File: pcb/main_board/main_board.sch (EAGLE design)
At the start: 30 parts, among them J1 5025700893, P1 53398-0510, P2 53398-0810, P3 53398-0410, U1 ATSAMD51J19A-AUT, U13 SPX3819-3.3, X2 32.768, X3 microUSB

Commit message: moved to feather wing design
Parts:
- removed C10: 1uF, rcl:C-EUC0603
- removed C6, C7, C8: 0.1uF, rcl:C-EUC0603
- removed C9: 0.01uF, rcl:C-EUC0603
- removed D1: MBR120, microbuilder:DIODE-SCHOTTKYSOD-123
- removed H1, H2, H3, H4: MOUNT-PAD-ROUND3.0, holes:MOUNT-PAD-ROUND3.0
- removed J1: 5025700893, 5025700893:5025700893
- removed L2: 10uH, microbuilder:INDUCTOR
- removed P2: 53398-0810, con-molex-picoblade:53398-0810
- removed P3: 53398-0410, con-molex-picoblade:53398-0410
- removed U$34: MAX3232E, TI_radio:MAX3232E
- removed X2: 32.768, adafruit2:XTAL-3.2X1.5
- removed X3: microUSB, microbuilder:USB_MICRO_20329_V2
- added C02_SERVO, IMU: 53398-0310, con-molex-picoblade:53398-0310
- added C14: 0.1uF, adafruit:C-USC0603
- added GPS, I2C, IRIDIUM: 53398-0410, con-molex-picoblade:53398-0410
- added JP1: (no value), microbuilder:HEADER-1X16ROUND
- added JP3: (no value), microbuilder:HEADER-1X12
- added PYRO, PYRO_BAT: 53398-0210, con-molex-picoblade:53398-0210
- added R3: 288, adafruit:R-US_R0603
- added SD_CARD: DM3CS-SF, DM3CS-SF:DM3CS-SF
- added TPMS: 53398-0610, con-molex-picoblade:53398-0610
- added U$1, U$7: AQV252GA, TI_radio:AQV252GA
- C1: value 1uF -> 0.1uF
- C2: value 10uF -> 0.1uF; device rcl:C-EUC0805 -> rcl:C-EUC0603
- C3, C4: value 22pF -> 0.1uF; device microbuilder:CAP_CERAMIC0603_NO -> rcl:C-EUC0603
- C5: device rcl:C-EUC0603 -> adafruit:C-USC0603
- R1: value 10k -> 288; device rcl:R-EU_R0603 -> adafruit:R-US_R0603
- U1: value ATSAMD51J19A-AUT -> ADM3101EARQZ-REELRQ_16_ADI-L; device ATSAMD51J19A-AUT:ATSAMD51J19A-AUT -> ADM310:ADM3101EARQZ-REELRQ_16_ADI-L
- renumbered P1 to TELEM
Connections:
- removed net 3.3V: C7.1, U$34.VCC
- removed net D+: U1.PA25/EIC/EXTINT[9], X3.D+
- removed net D-: U1.PA24/EIC/EXTINT[8], X3.D-
- removed net N$11: J1.DAT3/CD
- removed net N$12: J1.DAT2
- removed net N$13: J1.DAT1
- removed net N$14: J1.DAT0
- removed net N$15: TELEM.2
- removed net N$16: TELEM.3
- removed net N$17: TELEM.4
- removed net N$18: TELEM.5
- removed net N$19: H2.MOUNT
- removed net N$2: TELEM.1
- removed net N$20: H1.MOUNT
- removed net N$21: H4.MOUNT
- removed net N$22: H3.MOUNT
- removed net N$23: P2.1
- removed net N$24: P2.2
- removed net N$25: P2.3
- removed net N$26: P2.4
- removed net N$27: P2.5
- removed net N$28: P2.6
- removed net N$29: P2.7
- removed net N$30: P2.8
- removed net N$31: P3.1
- removed net N$32: P3.2
- removed net N$33: P3.3
- removed net N$34: P3.4
- removed net N$35: C5.1, U$34.C1+
- removed net N$36: C5.2, U$34.C1-
- removed net N$37: C8.1, U$34.C2+
- removed net N$38: C8.2, U$34.C2-
- removed net N$39: C9.1, U$34.V-
- removed net N$40: C6.1, U$34.V+
- removed net N$41: C10.2, U1.PA03/EIC/EXTINT[3]/ANAREF/VREFA/ADC0/ADIN[1]
- removed net N$5: C3.1, U1.PA00/EIC/EXTINT[0], X2.P$1
- removed net QSPI_CS: U1.PB11//EIC/EXTINT[11]
- removed net QSPI_DATA[0]: U1.PA08/EIC/NMI/ADC0/AIN[8]/ADC1/AIN[2]
- removed net QSPI_DATA[1]: U1.PA09/EIC/EXTINT[9]/ADC0/AIN[9]/ADC1/AIN[3]
- removed net QSPI_DATA[2]: U1.PA10//EIC/EXTINT[10]/ADC0/AIN[10]
- removed net QSPI_DATA[3]: U1.PA11/EIC/EXTINT[11]/ADC0/AIN[11]
- removed net QSPI_SCK: U1.PB10/EIC/EXTINT[10]
- removed net RX0: U1.PB17/EIC/EXTINT[1]
- removed net SD_DET: J1.DET_SW
- removed net SWCLK: U1.PA30//EIC/EXTINT[14]/X19/Y19
- removed net SWDIO: U1.PA31//EIC/EXTINT[15]
- removed net TX0: U1.PB16/EIC/EXTINT[0]
- new net !RESET: JP1.16
- new net 3V32: C29.1, C30.1, TELEM.4, U13.OUT
- new net 9V: PYRO_BAT.1, U$1.P$6
- new net AREF: JP1.14
- new net CO2_SERVO: C02_SERVO.1, JP3.6
- new net D5: JP3.10
- new net D6: JP3.9
- new net IR_ACT: JP3.7, R3.2
- new net LORA_RST: JP1.12, TELEM.1
- new net MISO: JP1.4, SD_CARD.DAT0
- new net MOSI: JP1.5, SD_CARD.CMD
- new net N$1: C5.1, R1.1, U$1.P$1
- new net N$6: C14.1, R3.1, U$7.P$1
- new net PYRO_ACT: JP3.8, R1.2
- new net RX4: JP1.11, TELEM.3
- new net SCHED: JP1.1, TPMS.2
- new net SCK: JP1.6, SD_CARD.CLK
- new net SCL: I2C.1, JP3.11
- new net SDA: I2C.2, JP3.12
- new net SD_CS: JP1.7, SD_CARD.CD/DAT3
- new net TX4: JP1.8, TELEM.2
- new net V+_IRIDIUM: IRIDIUM.3, U$7.P$4
- new net V+_PYRO: PYRO.1, U$1.P$4
- net 3V3: now also C4.2, GPS.3, I2C.3, JP1.15, SD_CARD.VDD, U1.VCC; no longer C29.1, C30.1, R1.2, U1.VDDANA, U1.VDDIO, U13.OUT
- net EN: now also IMU.1, JP3.2, TPMS.1
- net GND: now also C02_SERVO.3, C14.2, C5.2, GPS.4, I2C.4, IMU.3, IRIDIUM.4, JP1.13, PYRO.2, PYRO_BAT.2, SD_CARD.GND, SD_CARD.VSS, TELEM.5, TPMS.6, U$1.P$2, U$7.P$2; no longer C1.2, C10.1, C2.2, C4.2, C6.2, C7.2, C9.2, J1.DET_LEVER, J1.VSS, R1.1, U$34.GND, U1.RESETN, X3.GND
- net N$10: now also C2.2, U1.C2-; no longer J1.CMD
- net N$3: now also C4.1, U1.V+; no longer L2.1, U1.VSW
- net N$4: now also C3.1, U1.V-; no longer C1.1, C2.1, L2.2, U1.VDDCORE
- net N$7: now also C2.1, U1.C2+; no longer C4.1, U1.PA01/EIC/EXTINT[1], X2.P$2
- net N$8: now also C1.1, U1.C1+; no longer J1.VDD
- net N$9: now also C1.2, U1.C1-; no longer J1.CLK
- net R232: now also IRIDIUM.2, U1.RIN; no longer U$34.RI2
- net RIRI: now also JP3.4, U1.ROUT; no longer U$34.RO2
- net RX1: now also JP1.3, TPMS.4; no longer U1.PB09/EIC/EXTINT[9]/ADC0/AIN[3]/ADC1/AIN[1]
- net RX2: now also GPS.1, JP1.9; no longer U1.PA05//EIC/EXTINT[5]/ADC0/AIN[5]
- net T232: now also IRIDIUM.1, U1.TOUT; no longer U$34.DO2
- net TIRI: now also JP3.5, U1.TIN; no longer U$34.DI2
- net TX1: now also JP1.2, TPMS.3; no longer U1.PB08/EIC/EXTINT[8]/ADC0/AIN[2]/ADC1/AIN[0]
- net TX2: now also GPS.2, JP1.10; no longer U1.PA04/EIC/EXTINT[4]/ANAREF/VREFB/ADOC0/AIN[4]
- net VBAT: now also C02_SERVO.2, C22.1, IMU.2, JP3.1, R45.1, TPMS.5, U$7.P$6, U13.IN; no longer D1.A
- net VBUS: now also JP3.3; no longer C22.1, D1.C, R45.1, U13.IN, X3.VBUS
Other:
- note added: "BREAKOUTS"
- note added: "Solid State Relay"
- note removed: "3v3 ttl cons"
- note removed: "Iridium"
- note removed: "RS232 Connections"

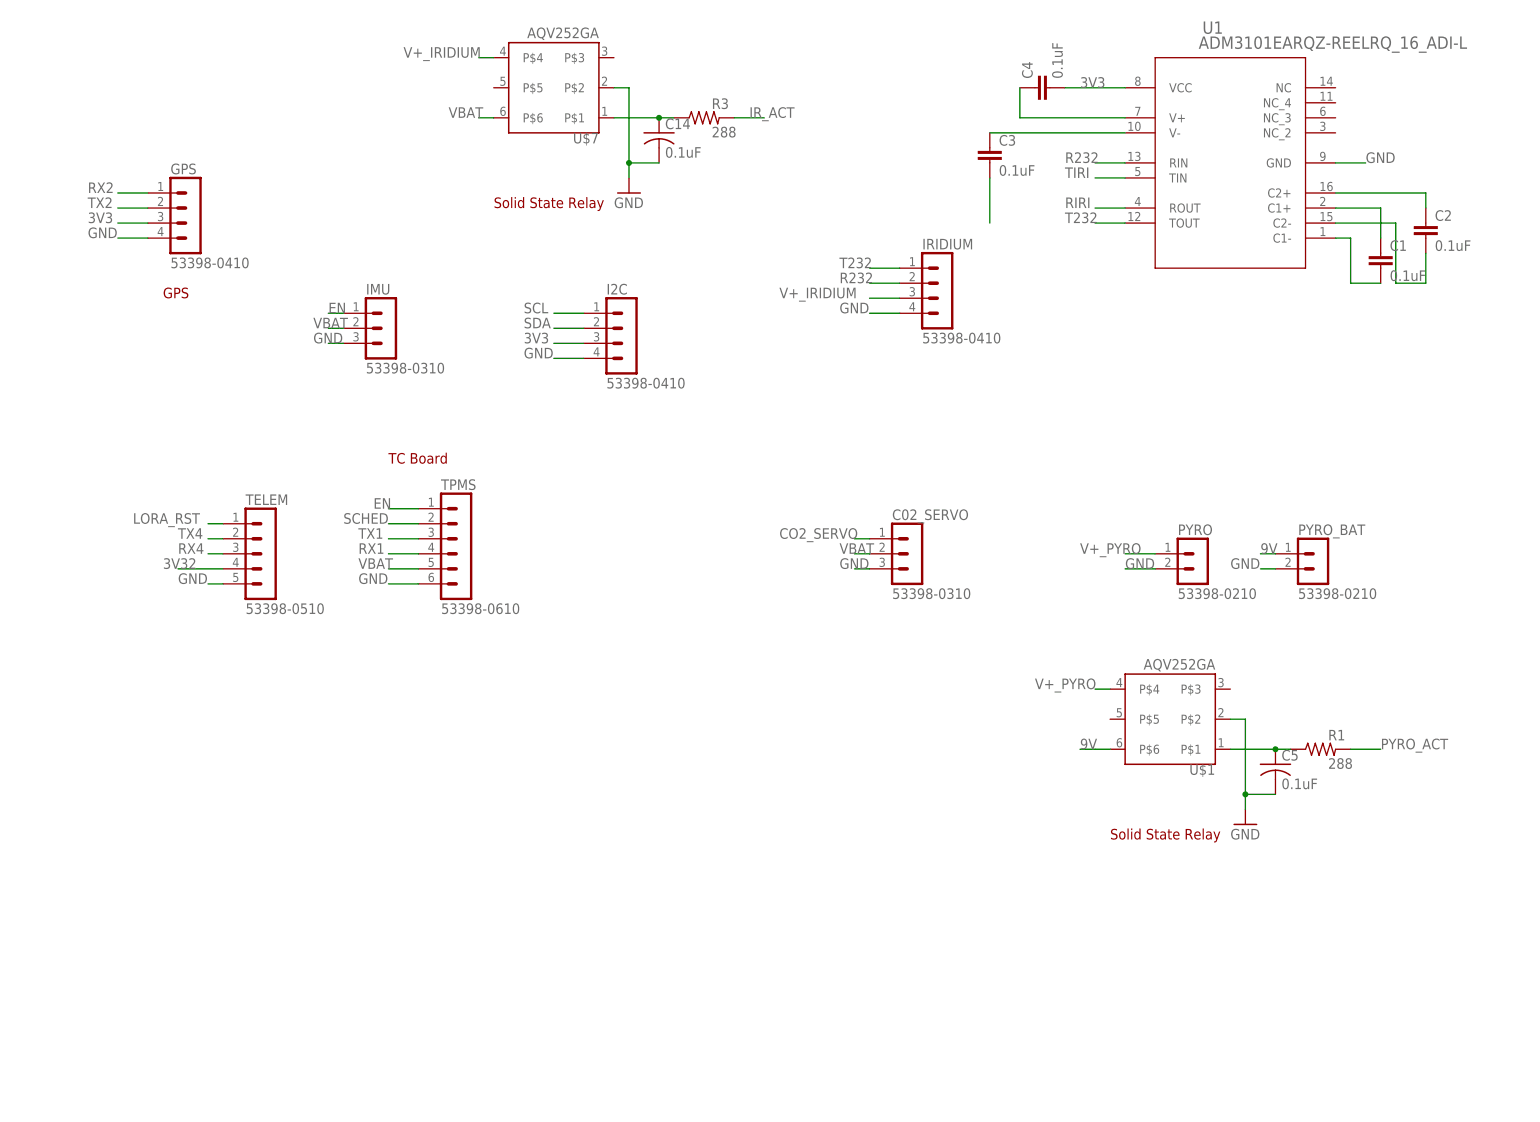
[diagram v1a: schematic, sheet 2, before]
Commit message: initial versions of imu logger, cdh, and tpms pcb
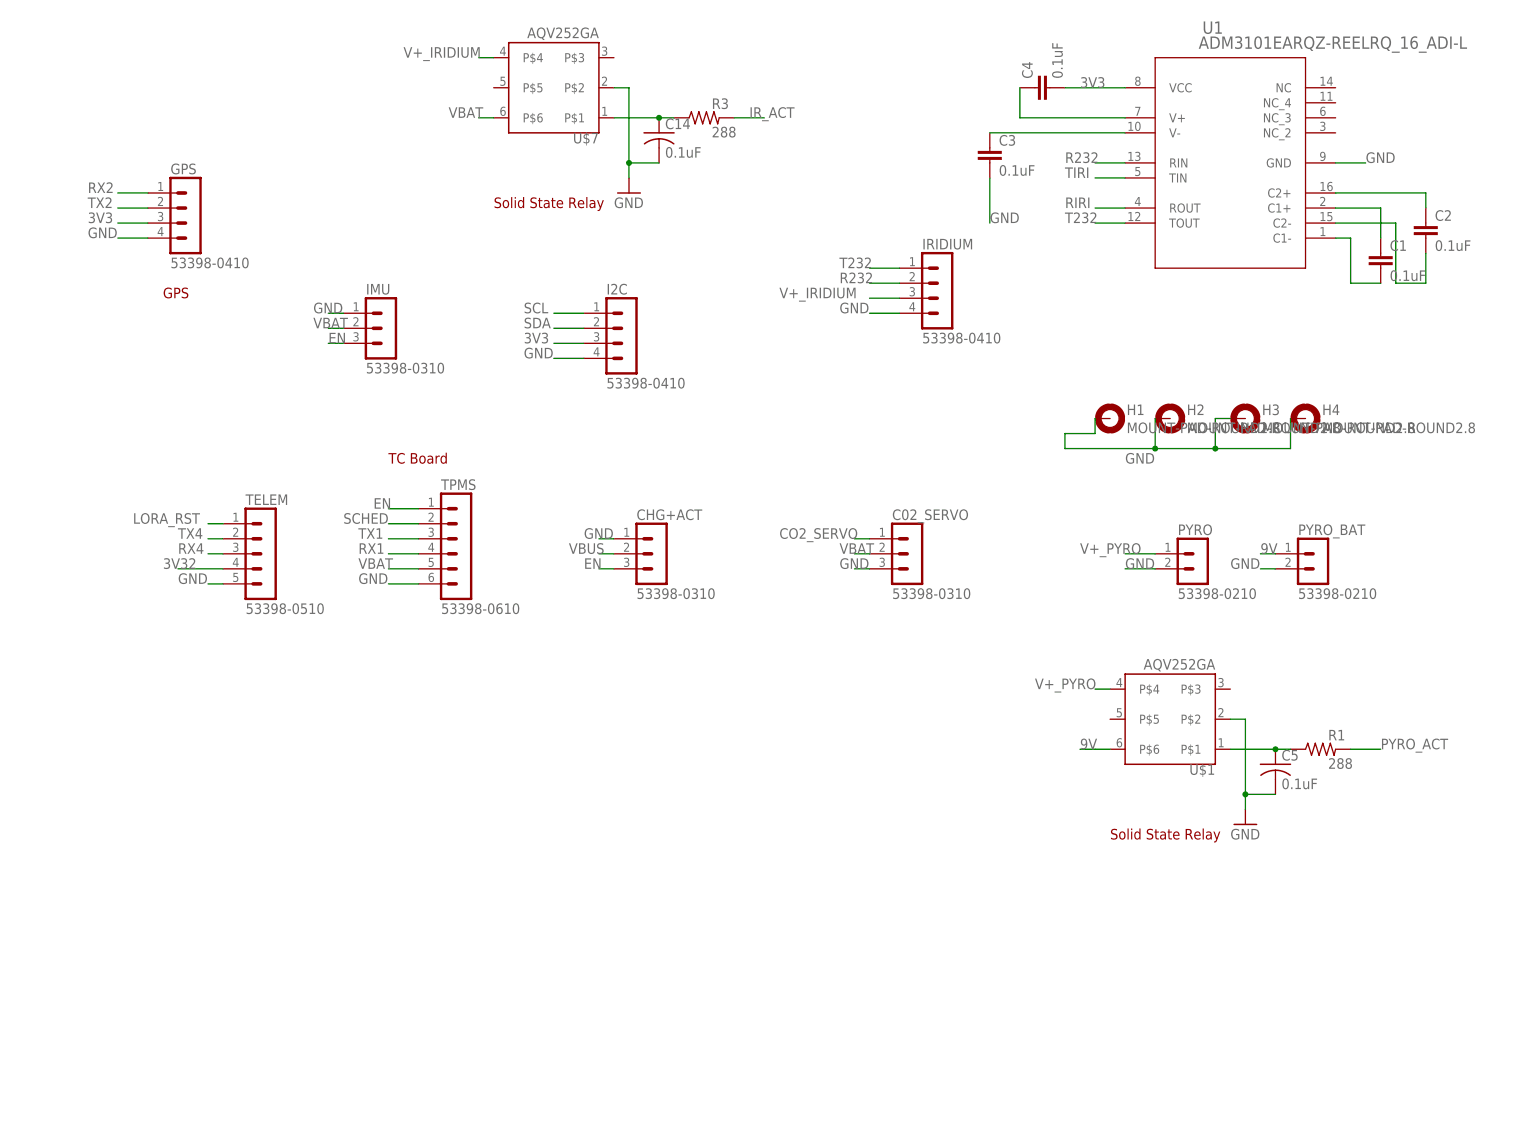
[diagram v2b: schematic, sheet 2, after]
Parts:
- added CHG+ACT: 53398-0310, con-molex-picoblade:53398-0310
- added H1, H2, H3, H4: MOUNT-PAD-ROUND2.8, holes:MOUNT-PAD-ROUND2.8
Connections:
- net EN: now also CHG+ACT.3, IMU.3; no longer IMU.1
- net GND: now also CHG+ACT.1, H1.MOUNT, H2.MOUNT, H3.MOUNT, H4.MOUNT, IMU.1; no longer IMU.3
- net VBUS: now also CHG+ACT.2
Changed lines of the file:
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@@
 <part name="U13" library="microbuilder" deviceset="VREG_SOT23-5" device="" value="SPX3819-3.3"/>
 <part name="R45" library="microbuilder" deviceset="RESISTOR" device="_0603_NOOUT" value="100k"/>
+<part name="H1" library="holes" library_urn="urn:adsk.eagle:library:237" deviceset="MOUNT-PAD-ROUND" device="2.8" package3d_urn="urn:adsk.eagle:package:14281/1"/>
+<part name="H2" library="holes" library_urn="urn:adsk.eagle:library:237" deviceset="MOUNT-PAD-ROUND" device="2.8" package3d_urn="urn:adsk.eagle:package:14281/1"/>
+<part name="H3" library="holes" library_urn="urn:adsk.eagle:library:237" deviceset="MOUNT-PAD-ROUND" device="2.8" package3d_urn="urn:adsk.eagle:package:14281/1"/>
+<part name="H4" library="holes" library_urn="urn:adsk.eagle:library:237" deviceset="MOUNT-PAD-ROUND" device="2.8" package3d_urn="urn:adsk.eagle:package:14281/1"/>
+<part name="CHG+ACT" library="con-molex-picoblade" library_urn="urn:adsk.eagle:library:28185481" deviceset="53398-0310" device="" package3d_urn="urn:adsk.eagle:package:28185543/1"/>
 </parts>
 <sheets>
@@
 <attribute name="VALUE" x="217.17" y="86.36" size="1.778" layer="95"/>
 </instance>
+<instance part="H1" gate="G$1" x="185.42" y="116.84" smashed="yes">
+<attribute name="NAME" x="188.214" y="117.4242" size="1.778" layer="95"/>
+<attribute name="VALUE" x="188.214" y="114.3762" size="1.778" layer="96"/>
+</instance>
+<instance part="H2" gate="G$1" x="195.58" y="116.84" smashed="yes">
+<attribute name="NAME" x="198.374" y="117.4242" size="1.778" layer="95"/>
+<attribute name="VALUE" x="198.374" y="114.3762" size="1.778" layer="96"/>
+</instance>
+<instance part="H3" gate="G$1" x="208.28" y="116.84" smashed="yes">
+<attribute name="NAME" x="211.074" y="117.4242" size="1.778" layer="95"/>
+<attribute name="VALUE" x="211.074" y="114.3762" size="1.778" layer="96"/>
+</instance>
+<instance part="H4" gate="G$1" x="218.44" y="116.84" smashed="yes">
+<attribute name="NAME" x="221.234" y="117.4242" size="1.778" layer="95"/>
+<attribute name="VALUE" x="221.234" y="114.3762" size="1.778" layer="96"/>
+</instance>
+<instance part="CHG+ACT" gate="G$1" x="106.68" y="93.98" smashed="yes">
+<attribute name="NAME" x="105.41" y="99.695" size="1.778" layer="95"/>
+<attribute name="VALUE" x="105.41" y="86.36" size="1.778" layer="95"/>
+</instance>
 </instances>
 <busses>
@@
 <pinref part="C3" gate="G$1" pin="2"/>
 <wire x1="165.1" y1="157.48" x2="165.1" y2="149.86" width="0.1524" layer="91"/>
+<label x="165.1" y="149.86" size="1.778" layer="95"/>
 </segment>
 <segment>
@@
 <wire x1="35.56" y1="88.9" x2="33.02" y2="88.9" width="0.1524" layer="91"/>
 <label x="27.94" y="88.9" size="1.778" layer="95"/>
-</segment>
-<segment>
-<pinref part="IMU" gate="G$1" pin="3"/>
-<wire x1="55.88" y1="129.54" x2="53.34" y2="129.54" width="0.1524" layer="91"/>
-<label x="50.8" y="129.54" size="1.778" layer="95"/>
 </segment>
 <segment>
@@
 <label x="205.74" y="91.44" size="1.778" layer="95"/>
 </segment>
+<segment>
+<pinref part="H1" gate="G$1" pin="MOUNT"/>
+<wire x1="182.88" y1="116.84" x2="182.88" y2="114.3" width="0.1524" layer="91"/>
+<wire x1="182.88" y1="114.3" x2="177.8" y2="114.3" width="0.1524" layer="91"/>
+<wire x1="177.8" y1="114.3" x2="177.8" y2="111.76" width="0.1524" layer="91"/>
+<wire x1="177.8" y1="111.76" x2="193.04" y2="111.76" width="0.1524" layer="91"/>
+<pinref part="H2" gate="G$1" pin="MOUNT"/>
+<wire x1="193.04" y1="111.76" x2="193.04" y2="116.84" width="0.1524" layer="91"/>
+<wire x1="193.04" y1="111.76" x2="203.2" y2="111.76" width="0.1524" layer="91"/>
+<junction x="193.04" y="111.76"/>
+<pinref part="H3" gate="G$1" pin="MOUNT"/>
+<wire x1="203.2" y1="111.76" x2="203.2" y2="116.84" width="0.1524" layer="91"/>
+<wire x1="203.2" y1="116.84" x2="205.74" y2="116.84" width="0.1524" layer="91"/>
+<wire x1="203.2" y1="111.76" x2="215.9" y2="111.76" width="0.1524" layer="91"/>
+<junction x="203.2" y="111.76"/>
+<pinref part="H4" gate="G$1" pin="MOUNT"/>
+<wire x1="215.9" y1="111.76" x2="215.9" y2="116.84" width="0.1524" layer="91"/>
+<label x="187.96" y="109.22" size="1.778" layer="95"/>
+</segment>
+<segment>
+<pinref part="IMU" gate="G$1" pin="1"/>
+<wire x1="55.88" y1="134.62" x2="53.34" y2="134.62" width="0.1524" layer="91"/>
+<label x="50.8" y="134.62" size="1.778" layer="95"/>
+</segment>
+<segment>
+<pinref part="CHG+ACT" gate="G$1" pin="1"/>
+<wire x1="101.6" y1="96.52" x2="99.06" y2="96.52" width="0.1524" layer="91"/>
+<label x="96.52" y="96.52" size="1.778" layer="95"/>
+</segment>
 </net>
 <net name="RIRI" class="0">
@@
 </segment>
 <segment>
-<pinref part="IMU" gate="G$1" pin="1"/>
-<wire x1="55.88" y1="134.62" x2="53.34" y2="134.62" width="0.1524" layer="91"/>
-<label x="53.34" y="134.62" size="1.778" layer="95"/>
+<pinref part="IMU" gate="G$1" pin="3"/>
+<wire x1="55.88" y1="129.54" x2="53.34" y2="129.54" width="0.1524" layer="91"/>
+<label x="53.34" y="129.54" size="1.778" layer="95"/>
+</segment>
+<segment>
+<pinref part="CHG+ACT" gate="G$1" pin="3"/>
+<wire x1="101.6" y1="91.44" x2="99.06" y2="91.44" width="0.1524" layer="91"/>
+<label x="96.52" y="91.44" size="1.778" layer="95"/>
 </segment>
 </net>
@@
 </segment>
 </net>
+<net name="VBUS" class="0">
+<segment>
+<pinref part="CHG+ACT" gate="G$1" pin="2"/>
+<wire x1="101.6" y1="93.98" x2="99.06" y2="93.98" width="0.1524" layer="91"/>
+<label x="93.98" y="93.98" size="1.778" layer="95"/>
+</segment>
+</net>

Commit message: finished TPMS board and other updates
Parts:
- removed SD_CARD: DM3CS-SF, DM3CS-SF:DM3CS-SF
- added J1: MEM2067-02-180-00-A_REVB, MEM20267:MEM2067-02-180-00-A_REVB
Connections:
- net 3V3: now also J1.VDD; no longer SD_CARD.VDD
- net GND: now also J1.SHIELD, J1.VSS; no longer SD_CARD.GND, SD_CARD.VSS
- net MISO: now also J1.DAT0; no longer SD_CARD.DAT0
- net MOSI: now also J1.CMD; no longer SD_CARD.CMD
- net SCK: now also J1.CLK; no longer SD_CARD.CLK
- net SD_CS: now also J1.CD/DAT3; no longer SD_CARD.CD/DAT3
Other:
- note added: "Activation and Charging"
- note added: "Barometer"
- note added: "Board to board connections"
- note added: "Extra 3v3 regulator"
- note added: "Feather M4 (SAMD51) headers"
- note added: "IMU"
- note added: "ISM Telem Radio"
- note added: "Iridium connector and power control"
- note added: "Mounting holes"
- note added: "Parachute CO2 and pyro controls and connectors"
- note added: "RS232 converter"
- note added: "SD Card"
